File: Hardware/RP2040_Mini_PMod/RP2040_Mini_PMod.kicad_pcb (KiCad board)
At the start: 4 copper layers, 40 x 20 mm, 44 parts, among them J1 Micro_SD_Card, J3 Conn_02x06_Odd_Even, J4 USB_C_Receptacle_USB2.0, SW1 PTS815 SJK 250 SMTR LFS, SW2 PTS815 SJK 250 SMTR LFS, U1 RP2040, U2 W25Q128JVS, U3 NCP1117-3.3_SOT223, Y1 12MHz

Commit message: add githash to back of PCB
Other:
- board text added: "SWCLK"
- board text added: "SWDIO"
- board text added: "Ver: %%GITHASH%%"
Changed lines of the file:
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@@
     (property "Sheetname" "")
     (attr exclude_from_pos_files)
-    (fp_text reference "TP2" (at 0.05 2.15 90) (layer "B.SilkS")
+    (fp_text reference "TP2" (at 0.05 2.15 90) (layer "B.SilkS") hide
       (effects (font (size 1 1) (thickness 0.15)) (justify mirror))
     )
@@
     (property "Sheetname" "")
     (attr exclude_from_pos_files)
-    (fp_text reference "TP1" (at 0.2 -1.95 90) (layer "B.SilkS")
+    (fp_text reference "TP1" (at 0.2 -1.95 90) (layer "B.SilkS") hide
       (effects (font (size 1 1) (thickness 0.15)) (justify mirror))
     )
@@
   (gr_arc (start 137 95) (mid 137.292893 94.292893) (end 138 94) (layer "Edge.Cuts") (width 0.1))
   (gr_line (start 138 114) (end 175.999999 113.999999) (layer "Edge.Cuts") (width 0.1))
+  (gr_text "Ver: %%GITHASH%%" (at 143 104 90) (layer "B.SilkS")
+    (effects (font (size 1 1) (thickness 0.1)) (justify mirror))
+  )
   (gr_text "RP2040 \nMini PMod\njjhorton.co.uk" (at 160.6 104.1 90) (layer "B.SilkS")
     (effects (font (size 1 1) (thickness 0.1)) (justify mirror))
   )
+  (gr_text "SWDIO" (at 153.5 113) (layer "B.SilkS")
+    (effects (font (size 1 1) (thickness 0.1)) (justify mirror))
+  )
+  (gr_text "SWCLK" (at 142.9 113) (layer "B.SilkS")
+    (effects (font (size 1 1) (thickness 0.1)) (justify mirror))
+  )

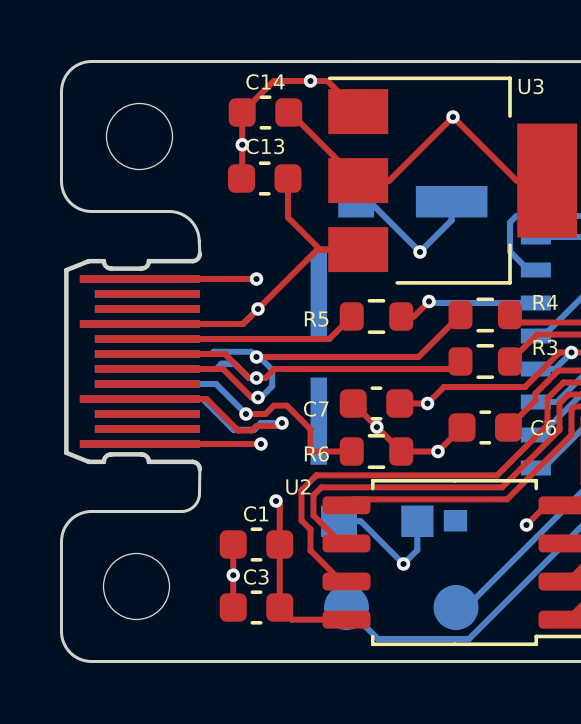
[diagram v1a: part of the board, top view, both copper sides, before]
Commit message: increase the space around the usb-c corrector
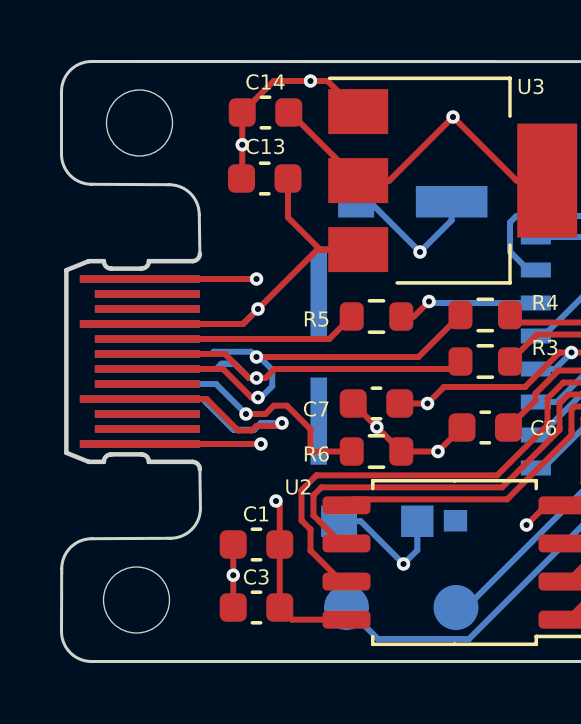
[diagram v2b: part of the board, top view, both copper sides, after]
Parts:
- moved REF** 0.45 mm to (139.6, 96.0)
- moved REF** 0.45 mm to (139.5, 112.0)
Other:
- outline, holes or cut-outs redrawn
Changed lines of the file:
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@@
   )
   (footprint "MountingHole:MountingHole_2.2mm_M2" (layer "F.Cu")
-    (at 139.6 96.5)
+    (at 139.6 96.05)
     (descr "Mounting Hole 2.2mm, no annular, M2")
     (tags "mounting hole 2.2mm no annular m2")
@@
   )
   (footprint "MountingHole:MountingHole_2.2mm_M2" (layer "F.Cu")
-    (at 139.5 111.5)
+    (at 139.5 111.95)
     (descr "Mounting Hole 2.2mm, no annular, M2")
     (tags "mounting hole 2.2mm no annular m2")
@@
   )
   (gr_line (start 175.992893 94.007107) (end 138 94) (layer "Edge.Cuts") (width 0.1))
-  (gr_arc (start 140.592893 99) (mid 141.3 99.292893) (end 141.592893 100) (layer "Edge.Cuts") (width 0.1))
-  (gr_line (start 141.6125 100.405) (end 141.592893 100) (layer "Edge.Cuts") (width 0.1))
+  (gr_arc (start 140.592893 98.107109) (mid 141.300004 98.4) (end 141.592893 99.107109) (layer "Edge.Cuts") (width 0.1))
+  (gr_line (start 141.6125 100.405) (end 141.592893 99.107109) (layer "Edge.Cuts") (width 0.1))
+  (gr_line (start 141.632107 108.892891) (end 141.6125 107.595) (layer "Edge.Cuts") (width 0.1))
   (gr_line (start 176.999999 112.999999) (end 176.992893 95.007107) (layer "Edge.Cuts") (width 0.1))
-  (gr_line (start 138 109) (end 141 109) (layer "Edge.Cuts") (width 0.1))
-  (gr_arc (start 141.6 108.4) (mid 141.424264 108.824264) (end 141 109) (layer "Edge.Cuts") (width 0.1))
-  (gr_line (start 141.6 108.4) (end 141.6125 107.595) (layer "Edge.Cuts") (width 0.1))
+  (gr_line (start 138.007107 109.907107) (end 140.632107 109.892891) (layer "Edge.Cuts") (width 0.1))
   (gr_arc (start 138 114) (mid 137.292893 113.707107) (end 137 113) (layer "Edge.Cuts") (width 0.1))
-  (gr_line (start 137 95) (end 137 98) (layer "Edge.Cuts") (width 0.1))
-  (gr_arc (start 137 110) (mid 137.292893 109.292893) (end 138 109) (layer "Edge.Cuts") (width 0.1))
-  (gr_line (start 137 113) (end 137 110) (layer "Edge.Cuts") (width 0.1))
-  (gr_arc (start 138 99) (mid 137.292893 98.707107) (end 137 98) (layer "Edge.Cuts") (width 0.1))
+  (gr_line (start 137 95) (end 137 97.092893) (layer "Edge.Cuts") (width 0.1))
+  (gr_arc (start 141.632107 108.892891) (mid 141.339217 109.600001) (end 140.632107 109.892891) (layer "Edge.Cuts") (width 0.1))
+  (gr_arc (start 137.007107 110.907107) (mid 137.3 110.2) (end 138.007107 109.907107) (layer "Edge.Cuts") (width 0.1))
+  (gr_line (start 137 113) (end 137.007107 110.907107) (layer "Edge.Cuts") (width 0.1))
+  (gr_arc (start 138 98.092893) (mid 137.292893 97.8) (end 137 97.092893) (layer "Edge.Cuts") (width 0.1))
   (gr_arc (start 175.992893 94.007107) (mid 176.7 94.3) (end 176.992893 95.007107) (layer "Edge.Cuts") (width 0.1))
-  (gr_line (start 140.592893 99) (end 138 99) (layer "Edge.Cuts") (width 0.1))
+  (gr_line (start 140.592893 98.107109) (end 138 98.092893) (layer "Edge.Cuts") (width 0.1))
   (gr_arc (start 176.999999 112.999999) (mid 176.707106 113.707106) (end 175.999999 113.999999) (layer "Edge.Cuts") (width 0.1))
   (gr_arc (start 137 95) (mid 137.292893 94.292893) (end 138 94) (layer "Edge.Cuts") (width 0.1))
@@
   )
   (dimension (type aligned) (layer "F.Cu")
-    (pts (xy 138.4 94) (xy 138.4 99))
-    (height 6.2)
-    (gr_text "5.0000 mm" (at 130.4 96.5 90) (layer "F.Cu")
+    (pts (xy 138.025736 109.9) (xy 138 114))
+    (height 2.926982)
+    (gr_text "4.1001 mm" (at 133.285979 111.920328 89.64035492) (layer "F.Cu")
       (effects (font (size 1.5 1.5) (thickness 0.3)))
     )
@@
   )
   (dimension (type aligned) (layer "F.Cu")
-    (pts (xy 137 114) (xy 137 109))
-    (height -6.2)
-    (gr_text "5.0000 mm" (at 129 111.5 90) (layer "F.Cu")
+    (pts (xy 138.4 94) (xy 138.4 98.1))
+    (height 6.2)
+    (gr_text "4.1000 mm" (at 130.4 96.05 90) (layer "F.Cu")
       (effects (font (size 1.5 1.5) (thickness 0.3)))
     )

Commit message: fix uneven sides of the usb connector
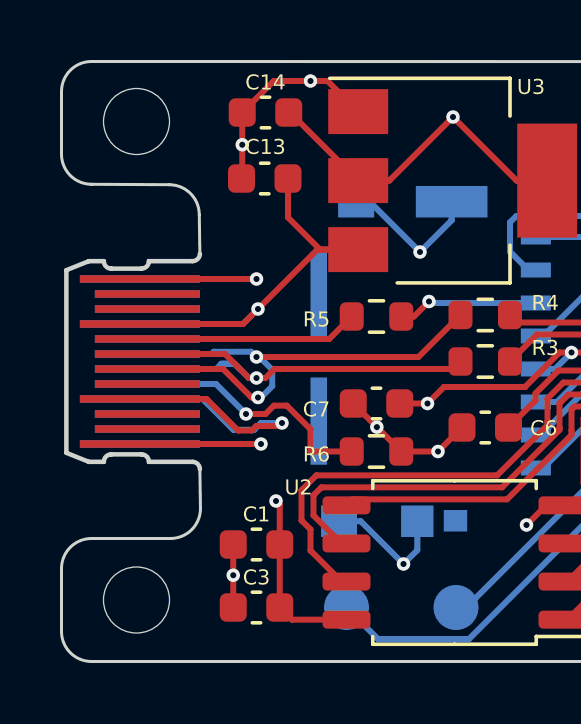
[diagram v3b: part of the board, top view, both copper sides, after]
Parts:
- moved REF** 0.11 mm to (139.5, 96.0)
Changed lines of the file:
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@@
   )
   (footprint "MountingHole:MountingHole_2.2mm_M2" (layer "F.Cu")
-    (at 139.6 96.05)
+    (at 139.5 96)
     (descr "Mounting Hole 2.2mm, no annular, M2")
     (tags "mounting hole 2.2mm no annular m2")
@@
   (gr_arc (start 140.592893 98.107109) (mid 141.300004 98.4) (end 141.592893 99.107109) (layer "Edge.Cuts") (width 0.1))
   (gr_line (start 141.6125 100.405) (end 141.592893 99.107109) (layer "Edge.Cuts") (width 0.1))
-  (gr_line (start 141.632107 108.892891) (end 141.6125 107.595) (layer "Edge.Cuts") (width 0.1))
+  (gr_line (start 141.632107 108.9) (end 141.6125 107.595) (layer "Edge.Cuts") (width 0.1))
   (gr_line (start 176.999999 112.999999) (end 176.992893 95.007107) (layer "Edge.Cuts") (width 0.1))
-  (gr_line (start 138.007107 109.907107) (end 140.632107 109.892891) (layer "Edge.Cuts") (width 0.1))
+  (gr_line (start 138 109.9) (end 140.632107 109.9) (layer "Edge.Cuts") (width 0.1))
   (gr_arc (start 138 114) (mid 137.292893 113.707107) (end 137 113) (layer "Edge.Cuts") (width 0.1))
   (gr_line (start 137 95) (end 137 97.092893) (layer "Edge.Cuts") (width 0.1))
-  (gr_arc (start 141.632107 108.892891) (mid 141.339217 109.600001) (end 140.632107 109.892891) (layer "Edge.Cuts") (width 0.1))
-  (gr_arc (start 137.007107 110.907107) (mid 137.3 110.2) (end 138.007107 109.907107) (layer "Edge.Cuts") (width 0.1))
-  (gr_line (start 137 113) (end 137.007107 110.907107) (layer "Edge.Cuts") (width 0.1))
+  (gr_arc (start 141.632107 108.9) (mid 141.339217 109.60711) (end 140.632107 109.9) (layer "Edge.Cuts") (width 0.1))
+  (gr_arc (start 137 110.9) (mid 137.292893 110.192893) (end 138 109.9) (layer "Edge.Cuts") (width 0.1))
+  (gr_line (start 137 113) (end 137 110.9) (layer "Edge.Cuts") (width 0.1))
   (gr_arc (start 138 98.092893) (mid 137.292893 97.8) (end 137 97.092893) (layer "Edge.Cuts") (width 0.1))
   (gr_arc (start 175.992893 94.007107) (mid 176.7 94.3) (end 176.992893 95.007107) (layer "Edge.Cuts") (width 0.1))
@@
     (effects (font (size 1 1) (thickness 0.1)) (justify mirror))
   )
-  (dimension (type aligned) (layer "F.Cu")
+  (dimension (type aligned) (layer "User.1")
     (pts (xy 137 114) (xy 137 94))
     (height -9.8)
-    (gr_text "20.0000 mm" (at 125.4 104 90) (layer "F.Cu")
+    (gr_text "20.0000 mm" (at 125.4 104 90) (layer "User.1")
       (effects (font (size 1.5 1.5) (thickness 0.3)))
     )
@@
     (style (thickness 0.2) (arrow_length 1.27) (text_position_mode 0) (extension_height 0.58642) (extension_offset 0.5) keep_text_aligned)
   )
-  (dimension (type aligned) (layer "F.Cu")
-    (pts (xy 138.025736 109.9) (xy 138 114))
+  (dimension (type aligned) (layer "User.1")
+    (pts (xy 138 109.9) (xy 138 114))
     (height 2.926982)
-    (gr_text "4.1001 mm" (at 133.285979 111.920328 89.64035492) (layer "F.Cu")
+    (gr_text "4.1000 mm" (at 133.273018 111.95 90) (layer "User.1")
       (effects (font (size 1.5 1.5) (thickness 0.3)))
     )
@@
     (style (thickness 0.2) (arrow_length 1.27) (text_position_mode 0) (extension_height 0.58642) (extension_offset 0.5) keep_text_aligned)
   )
-  (dimension (type aligned) (layer "F.Cu")
+  (dimension (type aligned) (layer "User.1")
     (pts (xy 138.4 94) (xy 138.4 98.1))
     (height 6.2)
-    (gr_text "4.1000 mm" (at 130.4 96.05 90) (layer "F.Cu")
+    (gr_text "4.1000 mm" (at 130.4 96.05 90) (layer "User.1")
       (effects (font (size 1.5 1.5) (thickness 0.3)))
     )
